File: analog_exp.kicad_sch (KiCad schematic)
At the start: 7 parts, among them J1 Conn_02x12_Odd_Even, J2 Conn_01x06, J3 Conn_01x06, J4 Conn_01x06, J5 Conn_01x06, J6 Conn_01x06, J7 Conn_01x06

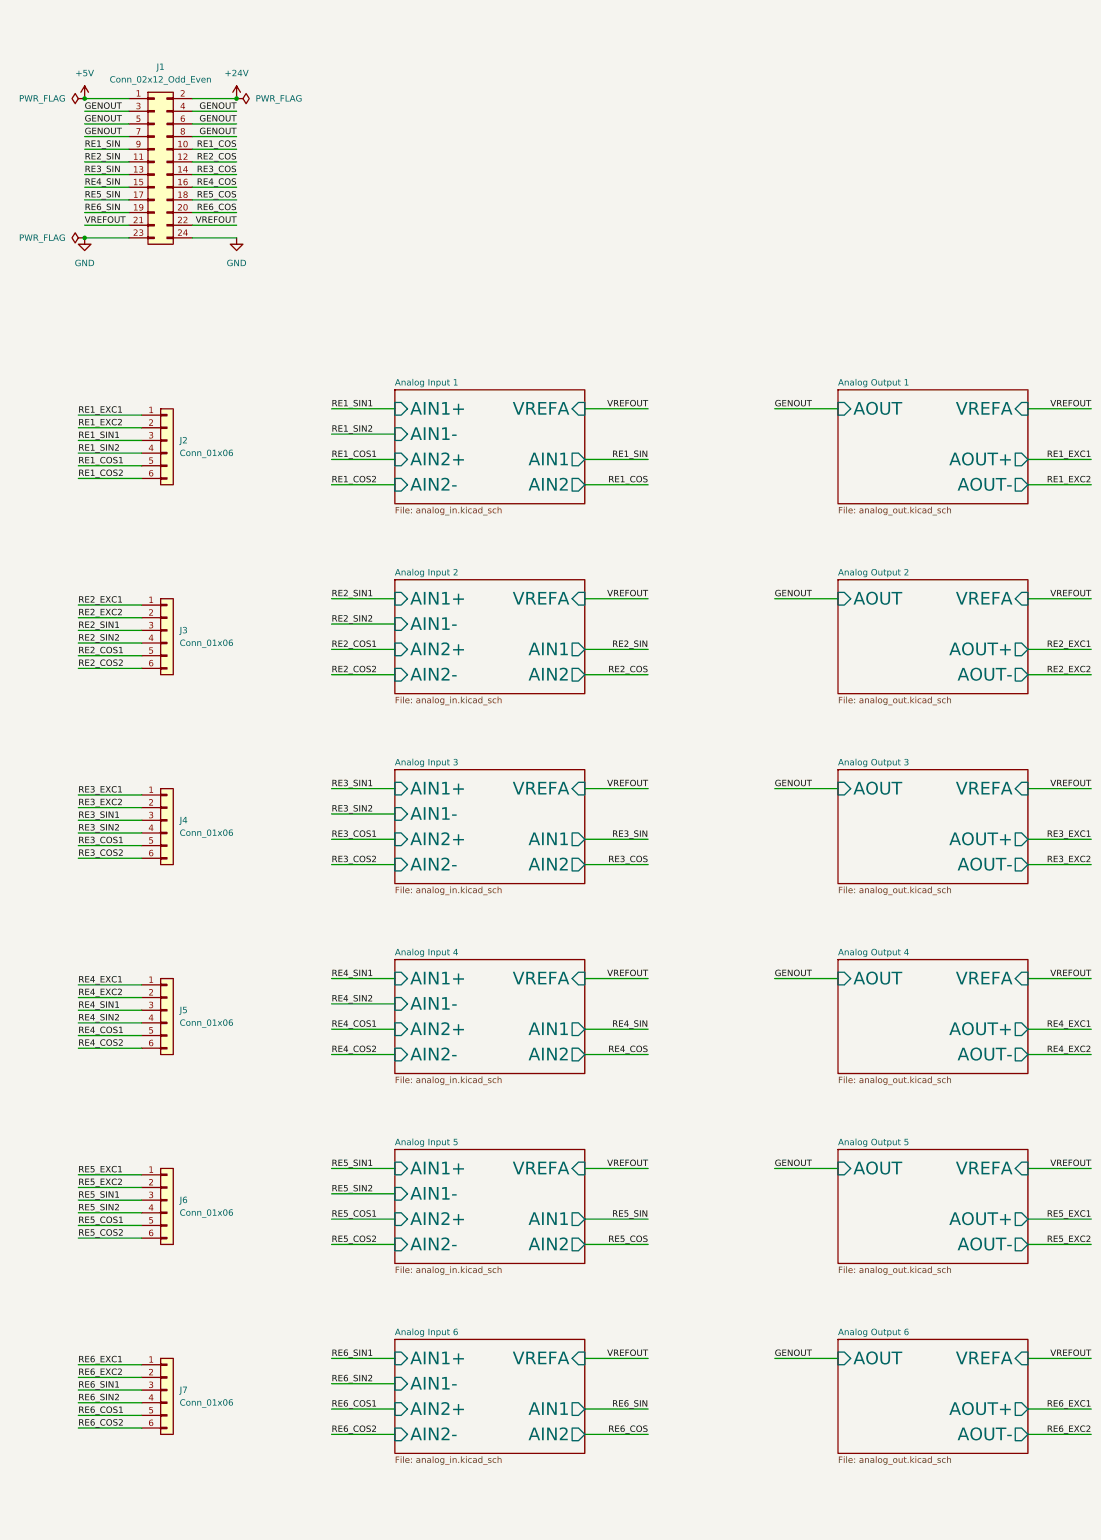
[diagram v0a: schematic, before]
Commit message: Added annotations and missing footprints
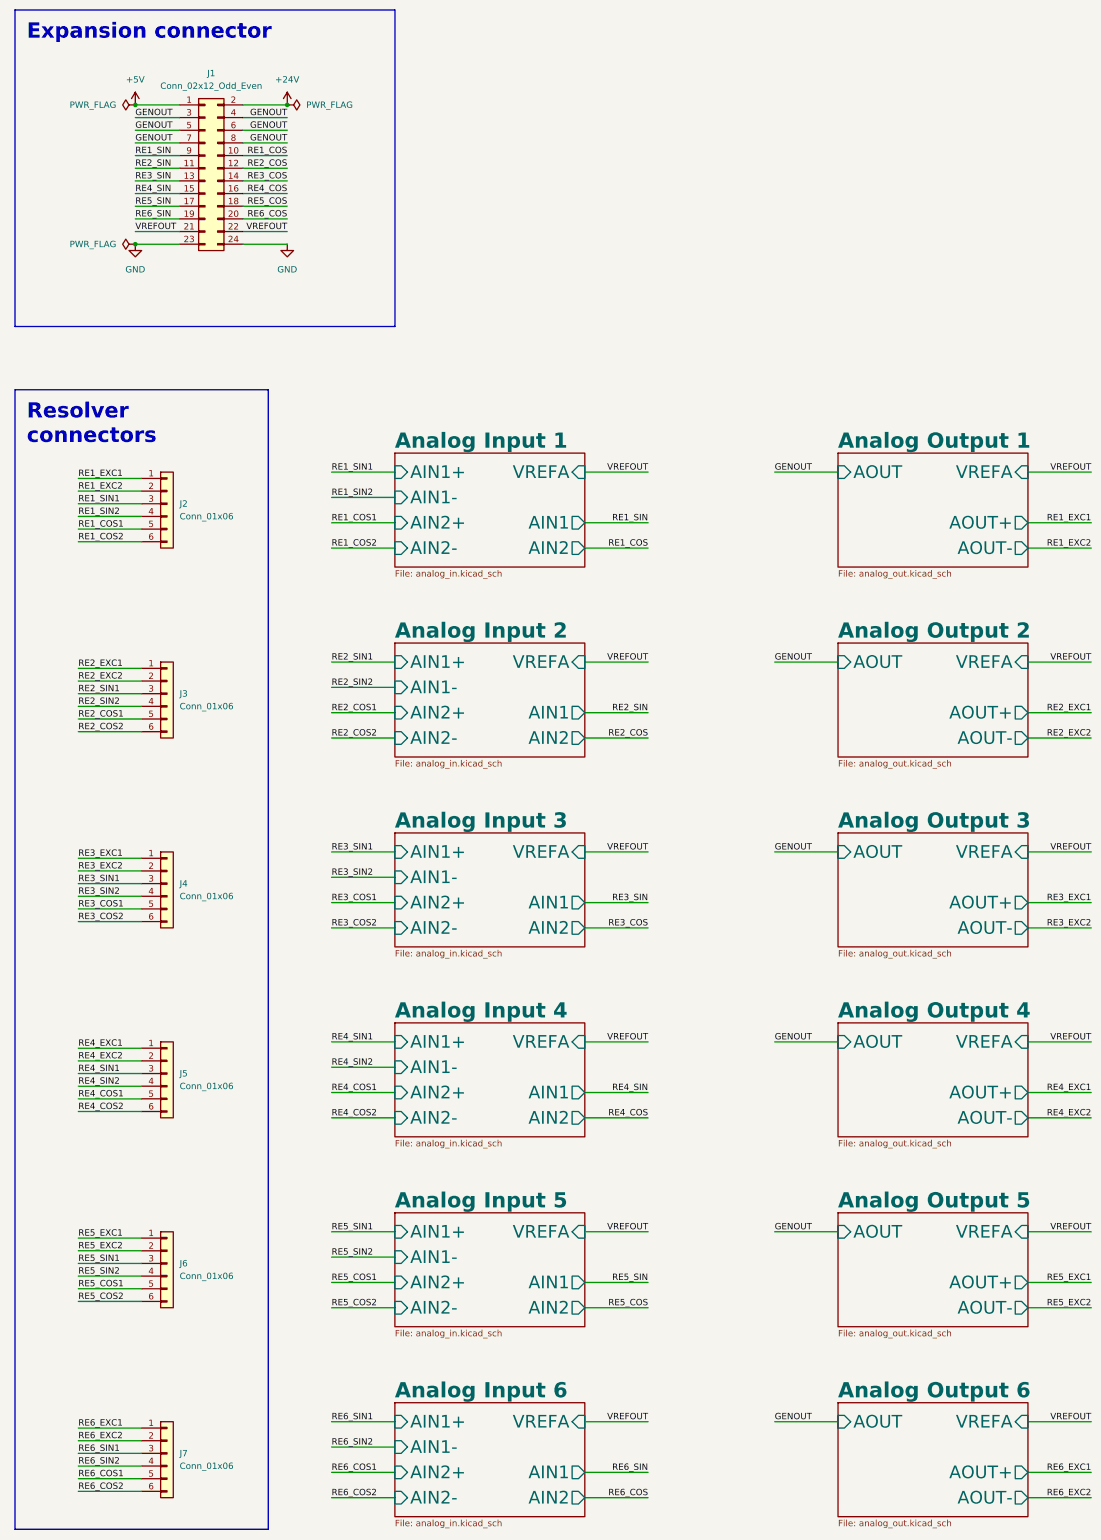
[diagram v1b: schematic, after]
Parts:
- J1: footprint (none) -> Connector_PinHeader_2.54mm:PinHeader_2x12_P2.54mm_Vertical
- J2, J3, J4, J5, J6, J7: footprint (none) -> Connector_JST:JST_PH_S6B-PH-SM4-TB_1x06-1MP_P2.00mm_Horizontal
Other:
- moved on the sheet: J1, J2, J3, J4, J5, J6, J7

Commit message: Assigned footprints for analog circuit
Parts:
- J1: value Conn_02x12_Odd_Even -> Pin Header; footprint Connector_PinHeader_2.54mm:PinHeader_2x12_P2.54mm_Vertical -> Connector_PinHeader_2.00mm:PinHeader_2x12_P2.00mm_Vertical
- J2, J3, J4, J5, J6, J7: value Conn_01x06 -> JST PH S6B; footprint Connector_JST:JST_PH_S6B-PH-SM4-TB_1x06-1MP_P2.00mm_Horizontal -> Connector_JST:JST_PH_S6B-PH-K_1x06_P2.00mm_Horizontal
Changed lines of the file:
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@@
       (effects (font (size 1.27 1.27)) (justify left))
     )
-    (property "Value" "Conn_01x06" (at 71.12 279.4 0)
-      (effects (font (size 1.27 1.27)) (justify left))
-    )
-    (property "Footprint" "Connector_JST:JST_PH_S6B-PH-SM4-TB_1x06-1MP_P2.00mm_Horizontal" (at 68.58 276.86 0)
+    (property "Value" "JST PH S6B" (at 71.12 279.4 0)
+      (effects (font (size 1.27 1.27)) (justify left))
+    )
+    (property "Footprint" "Connector_JST:JST_PH_S6B-PH-K_1x06_P2.00mm_Horizontal" (at 68.58 276.86 0)
       (effects (font (size 1.27 1.27)) hide)
     )
@@
       (effects (font (size 1.27 1.27)) (justify left))
     )
-    (property "Value" "Conn_01x06" (at 71.12 127 0)
-      (effects (font (size 1.27 1.27)) (justify left))
-    )
-    (property "Footprint" "Connector_JST:JST_PH_S6B-PH-SM4-TB_1x06-1MP_P2.00mm_Horizontal" (at 68.58 124.46 0)
+    (property "Value" "JST PH S6B" (at 71.12 127 0)
+      (effects (font (size 1.27 1.27)) (justify left))
+    )
+    (property "Footprint" "Connector_JST:JST_PH_S6B-PH-K_1x06_P2.00mm_Horizontal" (at 68.58 124.46 0)
       (effects (font (size 1.27 1.27)) hide)
     )
@@
   (symbol (lib_id "power:PWR_FLAG") (at 92.71 44.45 270) (unit 1)
     (in_bom yes) (on_board yes) (dnp no) (fields_autoplaced)
-    (property "Reference" "#FLG01" (at 94.615 44.45 0)
+    (property "Reference" "#FLG02" (at 94.615 44.45 0)
       (effects (font (size 1.27 1.27)) hide)
     )
@@
       (project "analog_exp"
         (path "/c77a085b-f0eb-4acf-9f36-7e73894837d0"
-          (reference "#FLG01") (unit 1)
+          (reference "#FLG02") (unit 1)
         )
       )
@@
       (effects (font (size 1.27 1.27)) (justify left))
     )
-    (property "Value" "Conn_01x06" (at 71.12 317.5 0)
-      (effects (font (size 1.27 1.27)) (justify left))
-    )
-    (property "Footprint" "Connector_JST:JST_PH_S6B-PH-SM4-TB_1x06-1MP_P2.00mm_Horizontal" (at 68.58 314.96 0)
+    (property "Value" "JST PH S6B" (at 71.12 317.5 0)
+      (effects (font (size 1.27 1.27)) (justify left))
+    )
+    (property "Footprint" "Connector_JST:JST_PH_S6B-PH-K_1x06_P2.00mm_Horizontal" (at 68.58 314.96 0)
       (effects (font (size 1.27 1.27)) hide)
     )
@@
       (effects (font (size 1.27 1.27)))
     )
-    (property "Value" "Conn_02x12_Odd_Even" (at 77.47 40.64 0)
-      (effects (font (size 1.27 1.27)))
-    )
-    (property "Footprint" "Connector_PinHeader_2.54mm:PinHeader_2x12_P2.54mm_Vertical" (at 76.2 57.15 0)
+    (property "Value" "Pin Header" (at 77.47 40.64 0)
+      (effects (font (size 1.27 1.27)))
+    )
+    (property "Footprint" "Connector_PinHeader_2.00mm:PinHeader_2x12_P2.00mm_Vertical" (at 76.2 57.15 0)
       (effects (font (size 1.27 1.27)) hide)
     )
@@
   (symbol (lib_id "power:PWR_FLAG") (at 62.23 44.45 90) (unit 1)
     (in_bom yes) (on_board yes) (dnp no) (fields_autoplaced)
-    (property "Reference" "#FLG02" (at 60.325 44.45 0)
+    (property "Reference" "#FLG01" (at 60.325 44.45 0)
       (effects (font (size 1.27 1.27)) hide)
     )
@@
       (project "analog_exp"
         (path "/c77a085b-f0eb-4acf-9f36-7e73894837d0"
-          (reference "#FLG02") (unit 1)
+          (reference "#FLG01") (unit 1)
         )
       )
@@
       (effects (font (size 1.27 1.27)) (justify left))
     )
-    (property "Value" "Conn_01x06" (at 71.12 165.1 0)
-      (effects (font (size 1.27 1.27)) (justify left))
-    )
-    (property "Footprint" "Connector_JST:JST_PH_S6B-PH-SM4-TB_1x06-1MP_P2.00mm_Horizontal" (at 68.58 162.56 0)
+    (property "Value" "JST PH S6B" (at 71.12 165.1 0)
+      (effects (font (size 1.27 1.27)) (justify left))
+    )
+    (property "Footprint" "Connector_JST:JST_PH_S6B-PH-K_1x06_P2.00mm_Horizontal" (at 68.58 162.56 0)
       (effects (font (size 1.27 1.27)) hide)
     )
@@
       (effects (font (size 1.27 1.27)) (justify left))
     )
-    (property "Value" "Conn_01x06" (at 71.12 203.2 0)
-      (effects (font (size 1.27 1.27)) (justify left))
-    )
-    (property "Footprint" "Connector_JST:JST_PH_S6B-PH-SM4-TB_1x06-1MP_P2.00mm_Horizontal" (at 68.58 200.66 0)
+    (property "Value" "JST PH S6B" (at 71.12 203.2 0)
+      (effects (font (size 1.27 1.27)) (justify left))
+    )
+    (property "Footprint" "Connector_JST:JST_PH_S6B-PH-K_1x06_P2.00mm_Horizontal" (at 68.58 200.66 0)
       (effects (font (size 1.27 1.27)) hide)
     )
@@
       (effects (font (size 1.27 1.27)) (justify left))
     )
-    (property "Value" "Conn_01x06" (at 71.12 241.3 0)
-      (effects (font (size 1.27 1.27)) (justify left))
-    )
-    (property "Footprint" "Connector_JST:JST_PH_S6B-PH-SM4-TB_1x06-1MP_P2.00mm_Horizontal" (at 68.58 238.76 0)
-      (effects (font (size 1.27 1.27)) hide)
-    )
+    (property "Value" "JST PH S6B" (at 71.12 241.3 0)
+      (effects (font (size 1.27 1.27)) (justify left))
+    )
+    (property "Footprint" "Connector_JST:JST_PH_S6B-PH-K_1x06_P2.00mm_Horizontal" (at 68.58 238.76 0)
+      (effects (font (size 1.27 1.27)) hide)
+    )

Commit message: Updated files to kicad 10
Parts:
- removed J1: Pin Header, Connector_PinHeader_2.00mm:PinHeader_2x12_P2.00mm_Vertical, symbol Connector_Generic:Conn_02x12_Odd_Even
- added J8: JST PHD B12B, Connector_JST:JST_PHD_B12B-PHDSS_2x06_P2.00mm_Vertical, symbol Connector_Generic:Conn_02x06_Odd_Even
- added J9: JST PH B4B, Connector_JST:JST_PH_B4B-PH-K_1x04_P2.00mm_Vertical, symbol Connector_Generic:Conn_01x04
- J2, J3, J4, J5, J6, J7: footprint Connector_JST:JST_PH_S6B-PH-K_1x06_P2.00mm_Horizontal -> Connector_JST:JST_PH_B6B-PH-K_1x06_P2.00mm_Vertical
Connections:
- net +5V: now also J8.1 (Pin_1), J8.11 (Pin_11), J8.3 (Pin_3), J8.5 (Pin_5), J8.7 (Pin_7), J8.9 (Pin_9)
- net GND: now also J8.10 (Pin_10), J8.12 (Pin_12), J8.2 (Pin_2), J8.4 (Pin_4), J8.6 (Pin_6), J8.8 (Pin_8), J9.4 (Pin_4)
- new net +3V3: J9.1 (Pin_1)
- new net SWDCLK: J9.2 (Pin_2)
- new net SWDIO: J9.3 (Pin_3)
- no-connect marks 0 -> 36
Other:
- added sheet Ethernet (ethernet.kicad_sch)
- added sheet Power Supply (power.kicad_sch)
- added sheet Transmitter (serializer.kicad_sch)
- moved on the sheet: J2, J3, J4, J5, J6, J7
